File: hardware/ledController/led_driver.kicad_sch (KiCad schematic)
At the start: 10 parts, among them Q1 FMMT458TA, Q2 BUJ302AD

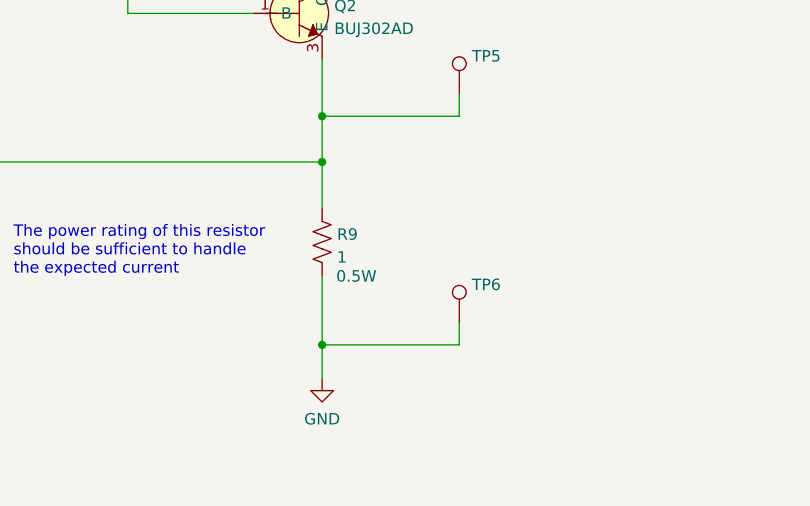
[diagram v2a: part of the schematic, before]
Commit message: Added NOLOAD resistor R10
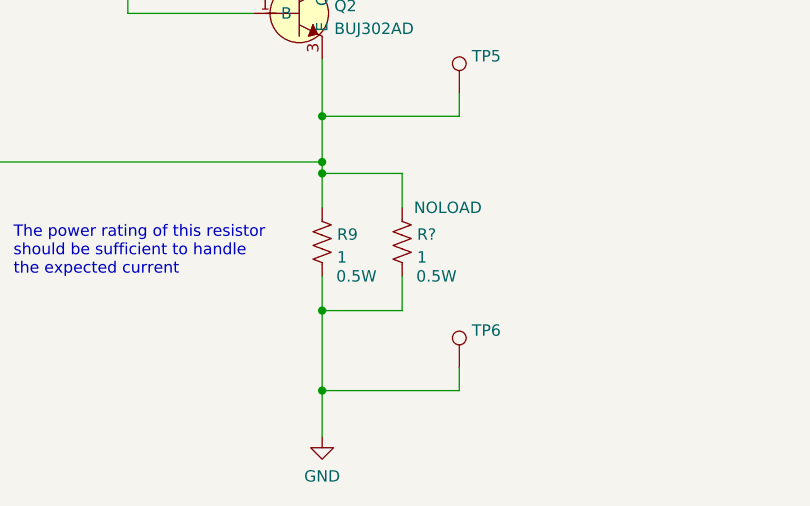
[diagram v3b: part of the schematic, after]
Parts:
- added R?: 1, Resistor_SMD:R_1210_3225Metric_Pad1.30x2.65mm_HandSolder, symbol Device:R_US
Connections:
- net GND: now also R?.2
- net at Q2.3 (E), R7.2, R9.1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: now also R?.1
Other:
- moved on the sheet: TP6
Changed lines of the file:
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@@
     (title "Lantern")
   )
+  (junction (at 142.24 127) (diameter 0) (color 0 0 0 0)
+  )
+  (junction (at 142.24 111.76) (diameter 0) (color 0 0 0 0)
+  )
   (junction (at 102.87 72.39) (diameter 0) (color 0 0 0 0)
   )
@@
   (junction (at 93.98 110.49) (diameter 0) (color 0 0 0 0)
   )
-  (junction (at 142.24 130.81) (diameter 0) (color 0 0 0 0)
-  )
   (junction (at 142.24 58.42) (diameter 0) (color 0 0 0 0)
   )
@@
   (junction (at 142.24 105.41) (diameter 0) (color 0 0 0 0)
   )
+  (junction (at 142.24 135.89) (diameter 0) (color 0 0 0 0)
+  )
   (wire (pts (xy 102.87 72.39) (xy 102.87 76.2))
     (stroke (width 0) (type default) (color 0 0 0 0))
   )
-  (wire (pts (xy 157.48 128.27) (xy 157.48 130.81))
+  (wire (pts (xy 151.13 127) (xy 142.24 127))
+    (stroke (width 0) (type default) (color 0 0 0 0))
+  )
+  (wire (pts (xy 157.48 133.35) (xy 157.48 135.89))
     (stroke (width 0) (type default) (color 0 0 0 0))
   )
@@
     (stroke (width 0) (type default) (color 0 0 0 0))
   )
+  (wire (pts (xy 151.13 115.57) (xy 151.13 111.76))
+    (stroke (width 0) (type default) (color 0 0 0 0))
+  )
   (wire (pts (xy 93.98 105.41) (xy 93.98 110.49))
     (stroke (width 0) (type default) (color 0 0 0 0))
@@
     (stroke (width 0) (type default) (color 0 0 0 0))
   )
+  (wire (pts (xy 142.24 111.76) (xy 151.13 111.76))
+    (stroke (width 0) (type default) (color 0 0 0 0))
+  )
   (wire (pts (xy 120.65 93.98) (xy 134.62 93.98))
     (stroke (width 0) (type default) (color 0 0 0 0))
@@
     (stroke (width 0) (type default) (color 0 0 0 0))
   )
-  (wire (pts (xy 142.24 130.81) (xy 157.48 130.81))
+  (wire (pts (xy 142.24 135.89) (xy 157.48 135.89))
     (stroke (width 0) (type default) (color 0 0 0 0))
   )
@@
     (stroke (width 0) (type default) (color 0 0 0 0))
   )
+  (wire (pts (xy 142.24 111.76) (xy 142.24 115.57))
+    (stroke (width 0) (type default) (color 0 0 0 0))
+  )
+  (wire (pts (xy 142.24 135.89) (xy 142.24 140.97))
+    (stroke (width 0) (type default) (color 0 0 0 0))
+  )
   (wire (pts (xy 102.87 83.82) (xy 102.87 87.63))
     (stroke (width 0) (type default) (color 0 0 0 0))
@@
     (stroke (width 0) (type default) (color 0 0 0 0))
   )
-  (wire (pts (xy 142.24 123.19) (xy 142.24 130.81))
-    (stroke (width 0) (type default) (color 0 0 0 0))
-  )
-  (wire (pts (xy 142.24 130.81) (xy 142.24 134.62))
+  (wire (pts (xy 142.24 123.19) (xy 142.24 127))
+    (stroke (width 0) (type default) (color 0 0 0 0))
+  )
+  (wire (pts (xy 142.24 127) (xy 142.24 135.89))
     (stroke (width 0) (type default) (color 0 0 0 0))
   )
@@
     (stroke (width 0) (type default) (color 0 0 0 0))
   )
-  (wire (pts (xy 142.24 110.49) (xy 142.24 115.57))
+  (wire (pts (xy 142.24 110.49) (xy 142.24 111.76))
+    (stroke (width 0) (type default) (color 0 0 0 0))
+  )
+  (wire (pts (xy 151.13 123.19) (xy 151.13 127))
     (stroke (width 0) (type default) (color 0 0 0 0))
   )
@@
     (pin "3")
   )
-  (symbol (lib_id "Connector:TestPoint") (at 157.48 128.27 0) (unit 1)
-    (in_bom yes) (on_board yes) (fields_autoplaced)
-    (property "Reference" "TP6" (id 0) (at 158.877 124.1333 0)
-      (effects (font (size 1.27 1.27)) (justify left))
-    )
-    (property "Value" "TestPoint" (id 1) (at 158.877 126.6702 0)
+  (symbol (lib_id "Connector:TestPoint") (at 157.48 133.35 0) (unit 1)
+    (in_bom yes) (on_board yes) (fields_autoplaced)
+    (property "Reference" "TP6" (id 0) (at 158.877 129.2133 0)
+      (effects (font (size 1.27 1.27)) (justify left))
+    )
+    (property "Value" "TestPoint" (id 1) (at 158.877 131.7502 0)
       (effects (font (size 1.27 1.27)) (justify left) hide)
     )
-    (property "Footprint" "TestPoint:TestPoint_Pad_D1.5mm" (id 2) (at 162.56 128.27 0)
-      (effects (font (size 1.27 1.27)) hide)
-    )
-    (property "Datasheet" "~" (id 3) (at 162.56 128.27 0)
-      (effects (font (size 1.27 1.27)) hide)
-    )
-    (pin "1")
-  )
-  (symbol (lib_id "power:GND") (at 142.24 134.62 0) (unit 1)
-    (in_bom yes) (on_board yes) (fields_autoplaced)
-    (property "Reference" "#PWR017" (id 0) (at 142.24 140.97 0)
-      (effects (font (size 1.27 1.27)) hide)
-    )
-    (property "Value" "GND" (id 1) (at 142.24 139.0634 0))
-    (property "Footprint" "" (id 2) (at 142.24 134.62 0)
-      (effects (font (size 1.27 1.27)) hide)
-    )
-    (property "Datasheet" "" (id 3) (at 142.24 134.62 0)
+    (property "Footprint" "TestPoint:TestPoint_Pad_D1.5mm" (id 2) (at 162.56 133.35 0)
+      (effects (font (size 1.27 1.27)) hide)
+    )
+    (property "Datasheet" "~" (id 3) (at 162.56 133.35 0)
+      (effects (font (size 1.27 1.27)) hide)
+    )
+    (pin "1")
+  )
+  (symbol (lib_id "power:GND") (at 142.24 140.97 0) (unit 1)
+    (in_bom yes) (on_board yes) (fields_autoplaced)
+    (property "Reference" "#PWR017" (id 0) (at 142.24 147.32 0)
+      (effects (font (size 1.27 1.27)) hide)
+    )
+    (property "Value" "GND" (id 1) (at 142.24 145.4134 0))
+    (property "Footprint" "" (id 2) (at 142.24 140.97 0)
+      (effects (font (size 1.27 1.27)) hide)
+    )
+    (property "Datasheet" "" (id 3) (at 142.24 140.97 0)
       (effects (font (size 1.27 1.27)) hide)
     )
@@
     (pin "1")
   )
+  (symbol (lib_id "Device:R_US") (at 151.13 119.38 0) (unit 1)
+    (in_bom yes) (on_board yes)
+    (property "Reference" "R?" (id 0) (at 152.781 118.5453 0)
+      (effects (font (size 1.27 1.27)) (justify left))
+    )
+    (property "Value" "1" (id 1) (at 152.781 121.0822 0)
+      (effects (font (size 1.27 1.27)) (justify left))
+    )
+    (property "Footprint" "Resistor_SMD:R_1210_3225Metric_Pad1.30x2.65mm_HandSolder" (id 2) (at 152.146 119.634 90)
+      (effects (font (size 1.27 1.27)) hide)
+    )
+    (property "Datasheet" "~" (id 3) (at 151.13 119.38 0)
+      (effects (font (size 1.27 1.27)) hide)
+    )
+    (property "Power" "0.5W" (id 4) (at 154.94 123.19 0))
+    (property "Field5" "NOLOAD" (id 5) (at 156.21 115.57 0))
+    (pin "1")
+    (pin "2")
+  )
   (symbol (lib_id "Device:R_US") (at 102.87 80.01 0) (unit 1)

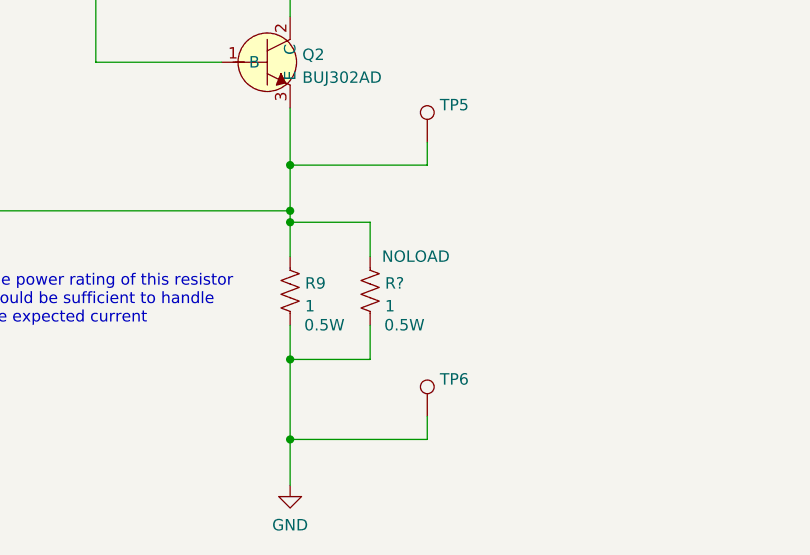
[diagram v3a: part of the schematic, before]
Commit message: First attempt of schematic to PCB
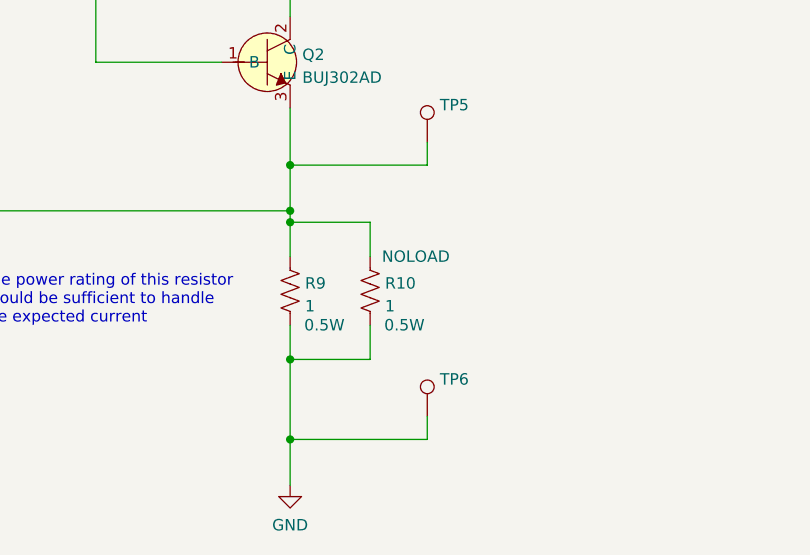
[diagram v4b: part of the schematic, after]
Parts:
- gave numbers to parts that had none: 1
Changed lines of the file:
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@@
   (symbol (lib_id "Device:R_US") (at 151.13 119.38 0) (unit 1)
     (in_bom yes) (on_board yes)
-    (property "Reference" "R?" (id 0) (at 152.781 118.5453 0)
+    (property "Reference" "R10" (id 0) (at 152.781 118.5453 0)
       (effects (font (size 1.27 1.27)) (justify left))
     )

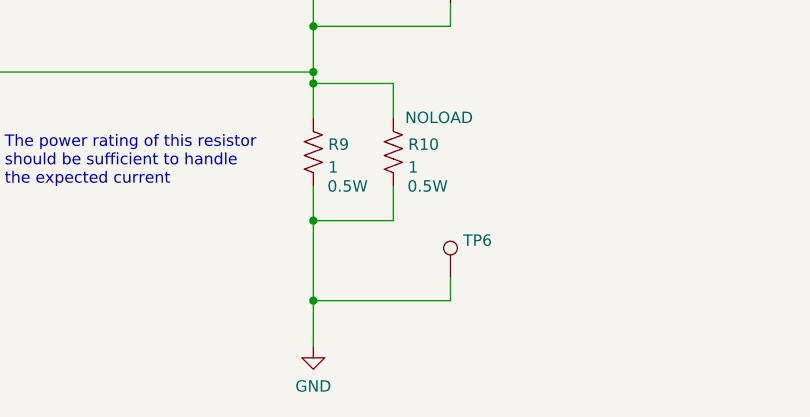
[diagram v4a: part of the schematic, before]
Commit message: More schematic updates
Moved from PIR sensor to photoresistor + additional components
Added mounting holes
Moved to a stand alone 3.3V switcher
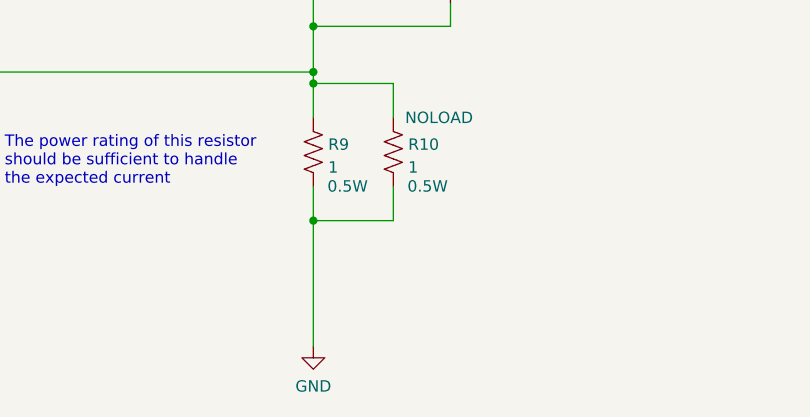
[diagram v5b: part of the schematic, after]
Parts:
- removed TP6: TestPoint, TestPoint:TestPoint_Pad_D1.5mm, symbol Connector:TestPoint
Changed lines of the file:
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@@
   (junction (at 142.24 105.41) (diameter 0) (color 0 0 0 0)
-  )
-  (junction (at 142.24 135.89) (diameter 0) (color 0 0 0 0)
   )
   (wire (pts (xy 102.87 72.39) (xy 102.87 76.2))
@@
   )
   (wire (pts (xy 151.13 127) (xy 142.24 127))
-    (stroke (width 0) (type default) (color 0 0 0 0))
-  )
-  (wire (pts (xy 157.48 133.35) (xy 157.48 135.89))
     (stroke (width 0) (type default) (color 0 0 0 0))
   )
@@
     (stroke (width 0) (type default) (color 0 0 0 0))
   )
-  (wire (pts (xy 142.24 135.89) (xy 157.48 135.89))
-    (stroke (width 0) (type default) (color 0 0 0 0))
-  )
   (wire (pts (xy 157.48 102.87) (xy 157.48 105.41))
     (stroke (width 0) (type default) (color 0 0 0 0))
@@
   )
   (wire (pts (xy 142.24 111.76) (xy 142.24 115.57))
-    (stroke (width 0) (type default) (color 0 0 0 0))
-  )
-  (wire (pts (xy 142.24 135.89) (xy 142.24 140.97))
     (stroke (width 0) (type default) (color 0 0 0 0))
   )
@@
     (stroke (width 0) (type default) (color 0 0 0 0))
   )
-  (wire (pts (xy 142.24 127) (xy 142.24 135.89))
+  (wire (pts (xy 142.24 127) (xy 142.24 140.97))
     (stroke (width 0) (type default) (color 0 0 0 0))
   )
@@
     (pin "3")
   )
-  (symbol (lib_id "Connector:TestPoint") (at 157.48 133.35 0) (unit 1)
-    (in_bom yes) (on_board yes) (fields_autoplaced)
-    (property "Reference" "TP6" (id 0) (at 158.877 129.2133 0)
-      (effects (font (size 1.27 1.27)) (justify left))
-    )
-    (property "Value" "TestPoint" (id 1) (at 158.877 131.7502 0)
-      (effects (font (size 1.27 1.27)) (justify left) hide)
-    )
-    (property "Footprint" "TestPoint:TestPoint_Pad_D1.5mm" (id 2) (at 162.56 133.35 0)
-      (effects (font (size 1.27 1.27)) hide)
-    )
-    (property "Datasheet" "~" (id 3) (at 162.56 133.35 0)
-      (effects (font (size 1.27 1.27)) hide)
-    )
-    (pin "1")
-  )
   (symbol (lib_id "power:GND") (at 142.24 140.97 0) (unit 1)

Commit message: Changed R9 and R10 to use 1206
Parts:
- R10, R9: footprint Resistor_SMD:R_1210_3225Metric_Pad1.30x2.65mm_HandSolder -> Resistor_SMD:R_1206_3216Metric_Pad1.30x1.75mm_HandSolder
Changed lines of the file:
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@@
       (effects (font (size 1.27 1.27)) (justify left))
     )
-    (property "Footprint" "Resistor_SMD:R_1210_3225Metric_Pad1.30x2.65mm_HandSolder" (id 2) (at 152.146 119.634 90)
+    (property "Footprint" "Resistor_SMD:R_1206_3216Metric_Pad1.30x1.75mm_HandSolder" (id 2) (at 152.146 119.634 90)
       (effects (font (size 1.27 1.27)) hide)
     )
@@
       (effects (font (size 1.27 1.27)) (justify left))
     )
-    (property "Footprint" "Resistor_SMD:R_1210_3225Metric_Pad1.30x2.65mm_HandSolder" (id 2) (at 143.256 119.634 90)
+    (property "Footprint" "Resistor_SMD:R_1206_3216Metric_Pad1.30x1.75mm_HandSolder" (id 2) (at 143.256 119.634 90)
       (effects (font (size 1.27 1.27)) hide)
     )

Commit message: Added comments
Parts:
- Q2: Power (none) -> 80W
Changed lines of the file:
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@@
   )
   (symbol (lib_id "ym_BJT:BUJ302AD") (at 139.7 93.98 0) (unit 1)
-    (in_bom yes) (on_board yes) (fields_autoplaced)
+    (in_bom yes) (on_board yes)
     (property "Reference" "Q2" (id 0) (at 143.5862 93.1453 0)
       (effects (font (size 1.27 1.27)) (justify left))
@@
       (effects (font (size 1.27 1.27)) hide)
     )
+    (property "Power" "80W" (id 4) (at 144.78 97.79 0))
     (pin "1")
     (pin "2")
